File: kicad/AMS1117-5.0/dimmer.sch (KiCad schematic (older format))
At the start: 9 parts, among them IC1 ATTINY85-S, P1 CONN_01X02, P2 CONN_01X02, Q1 Q_NMOS_GDS, SW2 TACTILE_SW, SW4 TACTILE_SW, U1 MC78L05ACH

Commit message: AMS1117-5.0 regulator version
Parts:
- U1: footprint TO_SOT_Packages_SMD:SOT89-3_Housing -> TO_SOT_Packages_SMD:SOT-223
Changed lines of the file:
@@
 F 0 "U1" H 2850 3300 50  0000 C CNN
 F 1 "MC78L05ACH" H 3050 3300 50  0000 L CNN
-F 2 "TO_SOT_Packages_SMD:SOT89-3_Housing" H 3050 3200 50  0001 C CIN
+F 2 "TO_SOT_Packages_SMD:SOT-223" H 3050 3200 50  0001 C CIN
 F 3 "" H 3050 3100 50  0000 C CNN
 	1    3050 3100

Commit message: AMS1117 correct footprint
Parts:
- added D1: D_Small, Diodes_SMD:DO-214BA, symbol D_Small
- U1: value MC78L05ACH -> AMS1117-5.0; footprint TO_SOT_Packages_SMD:SOT-223 -> Diodes_SMD:DO-214BA; symbol MC78L05ACH -> AP111750
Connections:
- net +12V: now also D1.2 (A); no longer U1.3 (IN)
- net +5V: now also U1.2 (VO), U1.4 (VO); no longer U1.1 (OUT)
- net GND: now also U1.1 (GND/ADJ); no longer U1.2 (GND)
- new net: D1.1 (K), U1.3 (VI)
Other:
- moved on the sheet: C1, P1, U1
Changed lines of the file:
@@
 L +12V #PWR02
 U 1 1 57A73161
-P 2550 2000
-F 0 "#PWR02" H 2550 1850 50  0001 C CNN
-F 1 "+12V" H 2550 2140 50  0000 C CNN
-F 2 "" H 2550 2000 50  0000 C CNN
-F 3 "" H 2550 2000 50  0000 C CNN
-	1    2550 2000
-	1    0    0    -1
-$EndComp
-$Comp
-L MC78L05ACH U1
+P 2500 2000
+F 0 "#PWR02" H 2500 1850 50  0001 C CNN
+F 1 "+12V" H 2500 2140 50  0000 C CNN
+F 2 "" H 2500 2000 50  0000 C CNN
+F 3 "" H 2500 2000 50  0000 C CNN
+	1    2500 2000
+	1    0    0    -1
+$EndComp
+$Comp
+L AP111750 U1
 U 1 1 57A7317B
-P 3050 3100
-F 0 "U1" H 2850 3300 50  0000 C CNN
-F 1 "MC78L05ACH" H 3050 3300 50  0000 L CNN
-F 2 "TO_SOT_Packages_SMD:SOT-223" H 3050 3200 50  0001 C CIN
-F 3 "" H 3050 3100 50  0000 C CNN
-	1    3050 3100
+P 3150 3050
+F 0 "U1" H 2950 3250 50  0000 C CNN
+F 1 "AMS1117-5.0" H 3150 3250 50  0000 L CNN
+F 2 "Diodes_SMD:DO-214BA" H 3150 3150 50  0001 C CIN
+F 3 "" H 3150 3050 50  0000 C CNN
+	1    3150 3050
 	1    0    0    -1
 $EndComp
@@
 L CONN_01X02 P1
 U 1 1 57A7320A
-P 2150 3100
-F 0 "P1" H 2150 3250 50  0000 C CNN
-F 1 "CONN_01X02" V 2250 3100 50  0000 C CNN
-F 2 "con-wago-508:W237-132" H 2150 3100 50  0001 C CNN
-F 3 "" H 2150 3100 50  0000 C CNN
-	1    2150 3100
+P 2100 3100
+F 0 "P1" H 2100 3250 50  0000 C CNN
+F 1 "CONN_01X02" V 2200 3100 50  0000 C CNN
+F 2 "con-wago-508:W237-132" H 2100 3100 50  0001 C CNN
+F 3 "" H 2100 3100 50  0000 C CNN
+	1    2100 3100
 	-1   0    0    1
 $EndComp
@@
 L C_Small C1
 U 1 1 57A73350
-P 2550 3250
-F 0 "C1" H 2560 3320 50  0000 L CNN
-F 1 "C_Small" H 2560 3170 50  0000 L CNN
-F 2 "Capacitors_SMD:C_0805" H 2550 3250 50  0001 C CNN
-F 3 "" H 2550 3250 50  0000 C CNN
-	1    2550 3250
+P 2500 3250
+F 0 "C1" H 2510 3320 50  0000 L CNN
+F 1 "C_Small" H 2510 3170 50  0000 L CNN
+F 2 "Capacitors_SMD:C_0805" H 2500 3250 50  0001 C CNN
+F 3 "" H 2500 3250 50  0000 C CNN
+	1    2500 3250
 	1    0    0    -1
 $EndComp
@@
 	3900 2850 3900 2000
 Wire Wire Line
-	2350 3050 2650 3050
-Wire Wire Line
-	2550 2000 2550 3150
-Connection ~ 2550 3050
-Wire Wire Line
-	2350 3150 2400 3150
-Wire Wire Line
-	2400 3150 2400 3450
-Wire Wire Line
-	3050 3350 3050 3450
+	2300 3050 2600 3050
+Wire Wire Line
+	2500 2000 2500 3150
+Connection ~ 2500 3050
+Wire Wire Line
+	2300 3150 2350 3150
+Wire Wire Line
+	2350 3150 2350 3450
+Wire Wire Line
+	3150 3350 3150 3450
 Wire Wire Line
 	3450 3050 3550 3050
@@
 	3550 3450 3550 3350
 Wire Wire Line
-	2550 3450 2550 3350
+	2500 3450 2500 3350
 Wire Wire Line
 	6600 3250 7700 3250
@@
 	8050 2950 8050 2750
 $Comp
-L +12V #PWR05
+L +12V #PWR04
 U 1 1 57A7493A
 P 8050 2000
-F 0 "#PWR05" H 8050 1850 50  0001 C CNN
+F 0 "#PWR04" H 8050 1850 50  0001 C CNN
 F 1 "+12V" H 8050 2140 50  0000 C CNN
 F 2 "" H 8050 2000 50  0000 C CNN
@@
 out
 $Comp
+L GND #PWR05
+U 1 1 57A75236
+P 2350 3450
+F 0 "#PWR05" H 2350 3200 50  0001 C CNN
+F 1 "GND" H 2350 3300 50  0000 C CNN
+F 2 "" H 2350 3450 50  0000 C CNN
+F 3 "" H 2350 3450 50  0000 C CNN
+	1    2350 3450
+	1    0    0    -1
+$EndComp
+$Comp
 L GND #PWR06
-U 1 1 57A75236
-P 2400 3450
-F 0 "#PWR06" H 2400 3200 50  0001 C CNN
-F 1 "GND" H 2400 3300 50  0000 C CNN
-F 2 "" H 2400 3450 50  0000 C CNN
-F 3 "" H 2400 3450 50  0000 C CNN
-	1    2400 3450
+U 1 1 57A7526C
+P 2500 3450
+F 0 "#PWR06" H 2500 3200 50  0001 C CNN
+F 1 "GND" H 2500 3300 50  0000 C CNN
+F 2 "" H 2500 3450 50  0000 C CNN
+F 3 "" H 2500 3450 50  0000 C CNN
+	1    2500 3450
 	1    0    0    -1
 $EndComp
 $Comp
 L GND #PWR07
-U 1 1 57A7526C
-P 2550 3450
-F 0 "#PWR07" H 2550 3200 50  0001 C CNN
-F 1 "GND" H 2550 3300 50  0000 C CNN
-F 2 "" H 2550 3450 50  0000 C CNN
-F 3 "" H 2550 3450 50  0000 C CNN
-	1    2550 3450
+U 1 1 57A7529B
+P 3150 3450
+F 0 "#PWR07" H 3150 3200 50  0001 C CNN
+F 1 "GND" H 3150 3300 50  0000 C CNN
+F 2 "" H 3150 3450 50  0000 C CNN
+F 3 "" H 3150 3450 50  0000 C CNN
+	1    3150 3450
 	1    0    0    -1
 $EndComp
 $Comp
 L GND #PWR08
-U 1 1 57A7529B
-P 3050 3450
-F 0 "#PWR08" H 3050 3200 50  0001 C CNN
-F 1 "GND" H 3050 3300 50  0000 C CNN
-F 2 "" H 3050 3450 50  0000 C CNN
-F 3 "" H 3050 3450 50  0000 C CNN
-	1    3050 3450
-	1    0    0    -1
-$EndComp
-$Comp
-L GND #PWR09
 U 1 1 57A752E2
 P 3550 3450
-F 0 "#PWR09" H 3550 3200 50  0001 C CNN
+F 0 "#PWR08" H 3550 3200 50  0001 C CNN
 F 1 "GND" H 3550 3300 50  0000 C CNN
 F 2 "" H 3550 3450 50  0000 C CNN
@@
 $EndComp
 $Comp
-L GND #PWR010
+L GND #PWR09
 U 1 1 57A75311
 P 3900 3450
-F 0 "#PWR010" H 3900 3200 50  0001 C CNN
+F 0 "#PWR09" H 3900 3200 50  0001 C CNN
 F 1 "GND" H 3900 3300 50  0000 C CNN
 F 2 "" H 3900 3450 50  0000 C CNN
@@
 $EndComp
 $Comp
-L GND #PWR011
+L GND #PWR010
 U 1 1 57A753DC
 P 7600 3450
-F 0 "#PWR011" H 7600 3200 50  0001 C CNN
+F 0 "#PWR010" H 7600 3200 50  0001 C CNN
 F 1 "GND" H 7600 3300 50  0000 C CNN
 F 2 "" H 7600 3450 50  0000 C CNN
@@
 $EndComp
 $Comp
-L GND #PWR012
+L GND #PWR011
 U 1 1 57A7540B
 P 8050 3450
-F 0 "#PWR012" H 8050 3200 50  0001 C CNN
+F 0 "#PWR011" H 8050 3200 50  0001 C CNN
 F 1 "GND" H 8050 3300 50  0000 C CNN
 F 2 "" H 8050 3450 50  0000 C CNN
@@
 	-1   0    0    -1
 $EndComp
+$Comp
+L D_Small D1
+U 1 1 58022341
+P 2700 3050
+F 0 "D1" H 2700 3345 50  0000 C CNN
+F 1 "D_Small" H 2700 3254 50  0000 C CNN
+F 2 "Diodes_SMD:DO-214BA" H 2700 3163 50  0000 C CNN
+F 3 "" V 2700 3050 50  0000 C CNN
+	1    2700 3050
+	-1   0    0    -1
+$EndComp
+Wire Wire Line
+	2800 3050 2850 3050
 $EndSCHEMATC

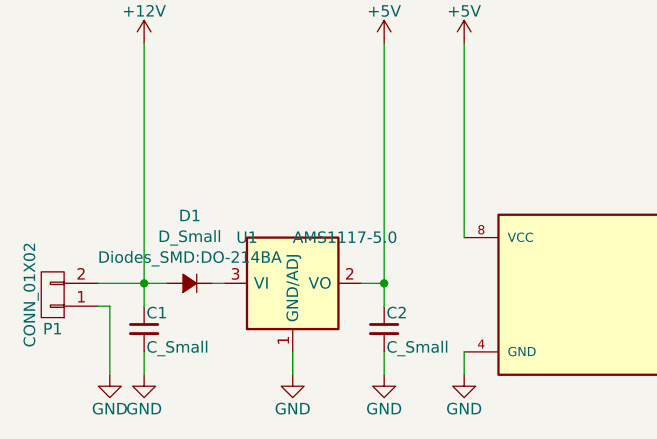
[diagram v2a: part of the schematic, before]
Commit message: AMS117 PCB version: fixed attyny85 footprint
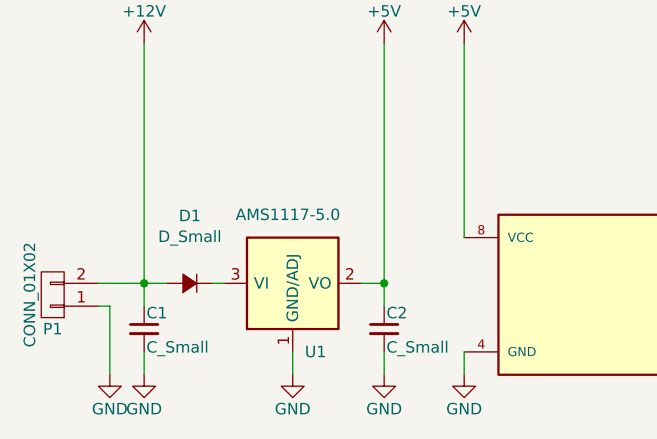
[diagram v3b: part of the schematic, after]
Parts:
- D1: footprint Diodes_SMD:DO-214BA -> Diodes_SMD:SMA_Standard
- U1: footprint Diodes_SMD:DO-214BA -> TO_SOT_Packages_SMD:SOT-223
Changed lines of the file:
@@
 EESchema Schematic File Version 2
-LIBS:power
-LIBS:device
-LIBS:transistors
-LIBS:conn
-LIBS:linear
-LIBS:regul
-LIBS:74xx
-LIBS:cmos4000
-LIBS:adc-dac
-LIBS:memory
-LIBS:xilinx
-LIBS:microcontrollers
-LIBS:dsp
-LIBS:microchip
-LIBS:analog_switches
-LIBS:motorola
-LIBS:texas
-LIBS:intel
-LIBS:audio
-LIBS:interface
-LIBS:digital-audio
-LIBS:philips
-LIBS:display
-LIBS:cypress
-LIBS:siliconi
-LIBS:opto
-LIBS:atmel
-LIBS:contrib
-LIBS:valves
-LIBS:irlz44nto220v
-LIBS:button
 LIBS:dimmer-cache
 EELAYER 25 0
@@
 U 1 1 57A7317B
 P 3150 3050
-F 0 "U1" H 2950 3250 50  0000 C CNN
-F 1 "AMS1117-5.0" H 3150 3250 50  0000 L CNN
-F 2 "Diodes_SMD:DO-214BA" H 3150 3150 50  0001 C CIN
+F 0 "U1" H 3250 2750 50  0000 C CNN
+F 1 "AMS1117-5.0" H 2900 3350 50  0000 L CNN
+F 2 "TO_SOT_Packages_SMD:SOT-223" H 3150 3150 50  0001 C CIN
 F 3 "" H 3150 3050 50  0000 C CNN
 	1    3150 3050
@@
 Connection ~ 7600 3050
 $Comp
+L D_Small D1
+U 1 1 58022341
+P 2700 3050
+F 0 "D1" H 2700 3345 50  0000 C CNN
+F 1 "D_Small" H 2700 3254 50  0000 C CNN
+F 2 "Diodes_SMD:SMA_Standard" H 2700 3163 50  0001 C CNN
+F 3 "" V 2700 3050 50  0000 C CNN
+	1    2700 3050
+	-1   0    0    -1
+$EndComp
+Wire Wire Line
+	2800 3050 2850 3050
+$Comp
 L ATTINY85-S IC1
-U 1 1 57AF71E0
+U 1 1 58047285
 P 5250 3100
 F 0 "IC1" H 5250 3707 50  0000 C CNN
@@
 	-1   0    0    -1
 $EndComp
-$Comp
-L D_Small D1
-U 1 1 58022341
-P 2700 3050
-F 0 "D1" H 2700 3345 50  0000 C CNN
-F 1 "D_Small" H 2700 3254 50  0000 C CNN
-F 2 "Diodes_SMD:DO-214BA" H 2700 3163 50  0000 C CNN
-F 3 "" V 2700 3050 50  0000 C CNN
-	1    2700 3050
-	-1   0    0    -1
-$EndComp
-Wire Wire Line
-	2800 3050 2850 3050
 $EndSCHEMATC
